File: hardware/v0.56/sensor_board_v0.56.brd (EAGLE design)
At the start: 50.8 x 50.8 mm, 69 parts, among them J3 USB-MICROB, U1 NEOPIXEL_NANO_2427, U10 TSL2591, U11 915MHz, U12 MH-Z19, U13 CCS811-I2C, U14 IAQ-CORE-C, U15 VLP-450-F, U16 VLP-450-F, U2 FT231XQ-R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

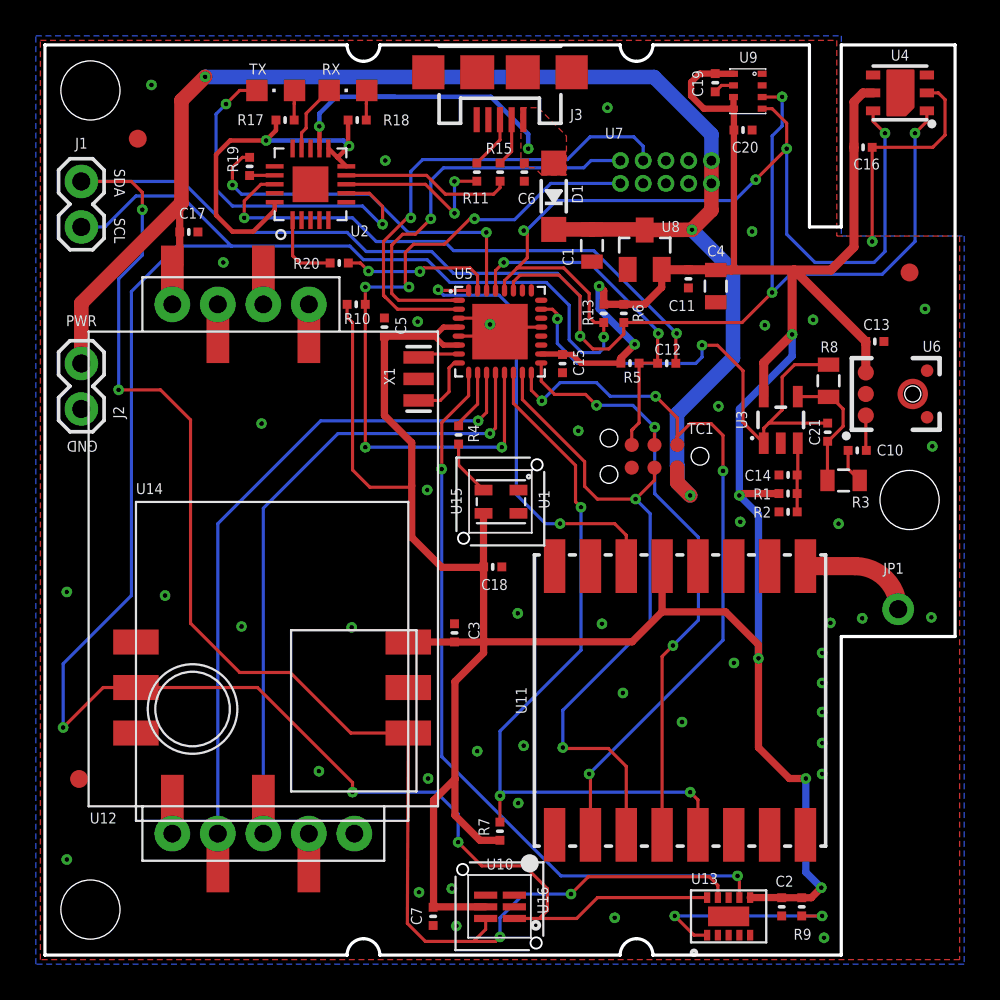
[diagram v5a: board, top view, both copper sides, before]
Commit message: v0.56b - minor update
silkscreen update and a couple of traces
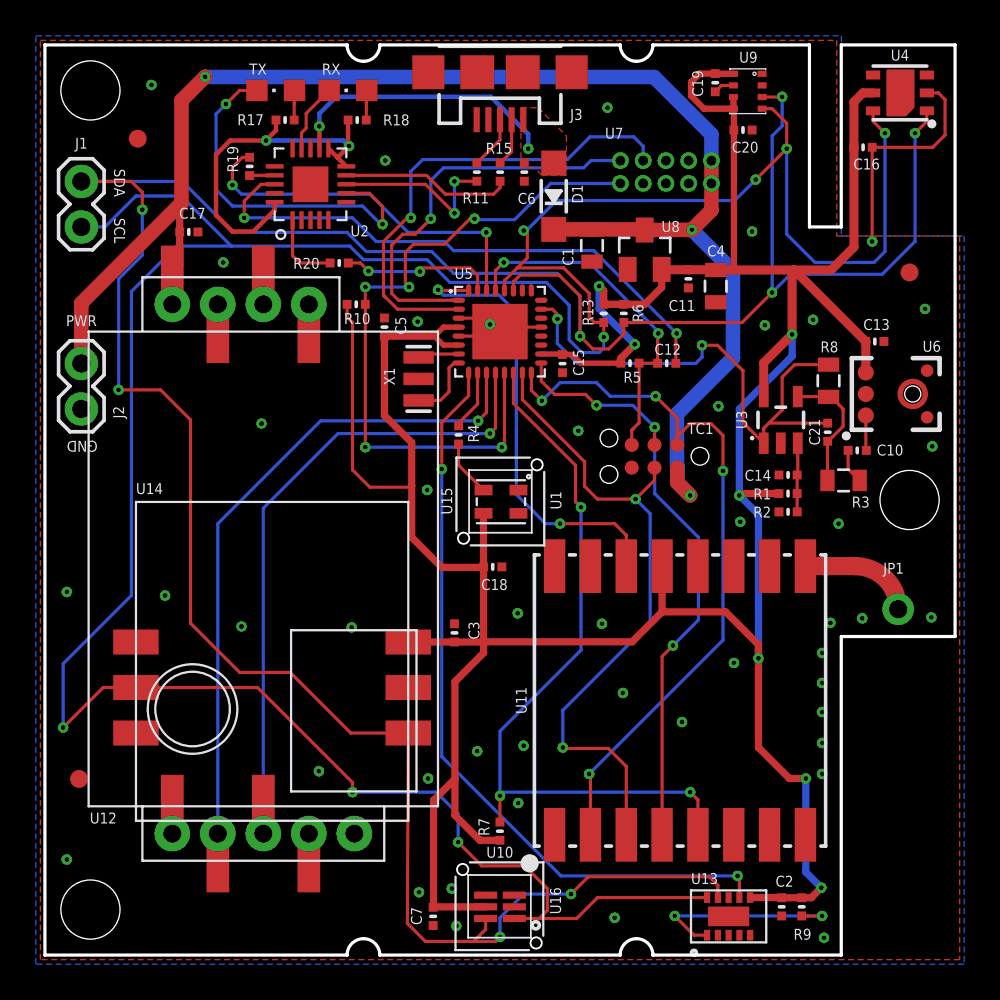
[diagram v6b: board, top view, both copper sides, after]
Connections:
- removed net N$12: U$4.P$4
- removed net N$14: U$5.P$1
- removed net N$19: U$5.P$4
- removed net N$8: U$4.P$3
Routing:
- net VBUS: track 17.8 -> 15.7 mm
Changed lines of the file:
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@@
 <element name="U10" library="TSL2591" package="DFN6_TAOS" value="TSL2591" x="25.4" y="2.6924" smashed="yes" rot="R180">
 <attribute name="MPN" value="TSL25911FN " x="25.4" y="2.6924" size="1.778" layer="27" rot="R180" display="off"/>
-<attribute name="NAME" x="24.638" y="4.7736" size="0.6096" layer="121" font="vector"/>
+<attribute name="NAME" x="24.638" y="5.434" size="0.6096" layer="121" font="vector"/>
 </element>
 <element name="J1" library="SparkFun-Connectors" package="1X02" value="" x="2.032" y="40.64" smashed="yes" rot="R90">
@@
 </element>
 <element name="U1" library="NeoPixel Nano 2427" package="SK6805-2427" value="NEOPIXEL_NANO_2427" x="24.1046" y="24.1046" smashed="yes">
-<attribute name="NAME" x="28.1686" y="24.9174" size="0.6096" layer="121" font="vector" rot="R90"/>
+<attribute name="NAME" x="28.829" y="24.8666" size="0.6096" layer="121" font="vector" rot="R90"/>
 </element>
 <element name="C18" library="Adafruit Feather 32u4 Bluefruit LE" package="MICROBUILDER__0402MP" value="1uF" x="24.9936" y="21.6662" smashed="yes" rot="R180">
@@
 </element>
 <element name="U15" library="VLP-450-F" package="VLP-450-F" value="VLP-450-F" x="23.368" y="23.2664" smashed="yes">
-<attribute name="NAME" x="23.2664" y="24.5872" size="0.6096" layer="121" font="vector" rot="R90"/>
+<attribute name="NAME" x="22.733" y="24.5872" size="0.6096" layer="121" font="vector" rot="R90"/>
 </element>
 <element name="U16" library="VLP-450-F" package="VLP-450-F" value="VLP-450-F" x="23.3172" y="4.7752" smashed="yes" rot="R270">
-<attribute name="NAME" x="27.4828" y="3.81" size="0.6096" layer="121" font="vector" rot="R270"/>
+<attribute name="NAME" x="28.194" y="3.7846" size="0.6096" layer="121" font="vector" rot="R270"/>
 </element>
 <element name="C5" library="Adafruit Feather 32u4 Bluefruit LE" package="MICROBUILDER__0402MP" value="0.1uF" x="18.9484" y="35.052" smashed="yes" rot="R270">
@@
 <vertex x="26.5684" y="43.942"/>
 </polygon>
-<wire x1="17.4752" y1="47.9044" x2="24.892" y2="47.9044" width="0.254" layer="16"/>
 <wire x1="26.9748" y1="45.0088" x2="26.9748" y2="45.8216" width="0.254" layer="16"/>
 <wire x1="26.9748" y1="45.8216" x2="24.892" y2="47.9044" width="0.254" layer="16"/>
 <wire x1="15.3232" y1="45.021" x2="15.3232" y2="46.2464" width="0.254" layer="1"/>
 <wire x1="15.3232" y1="46.2464" x2="15.3162" y2="46.2534" width="0.254" layer="1"/>
-<wire x1="16.256" y1="47.9044" x2="19.5326" y2="47.9044" width="0.254" layer="16"/>
-<wire x1="15.3162" y1="46.2534" x2="15.3162" y2="46.9646" width="0.254" layer="16"/>
-<wire x1="15.3162" y1="46.9646" x2="16.256" y2="47.9044" width="0.254" layer="16"/>
-<wire x1="17.4752" y1="47.9044" x2="16.256" y2="47.9044" width="0" layer="19" extent="16-16"/>
+<wire x1="15.3162" y1="46.9646" x2="15.3162" y2="46.2534" width="0.254" layer="16"/>
+<wire x1="24.892" y1="47.9044" x2="16.256" y2="47.9044" width="0.254" layer="16"/>
+<wire x1="16.256" y1="47.9044" x2="15.3162" y2="46.9646" width="0.254" layer="16"/>
 </signal>
 <signal name="N$32">
@@
 <wire x1="45.2196" y1="21.7094" x2="47.625" y2="19.304" width="1.016" layer="1" curve="-90"/>
 </signal>
-<signal name="N$8">
-<contactref element="U$4" pad="P$3"/>
-</signal>
-<signal name="N$12">
-<contactref element="U$4" pad="P$4"/>
-</signal>
-<signal name="N$14">
-<contactref element="U$5" pad="P$1"/>
-</signal>
-<signal name="N$19">
-<contactref element="U$5" pad="P$4"/>
-</signal>
 </signals>

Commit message: Shifted radio a bit
to allow space for the light pipe to land
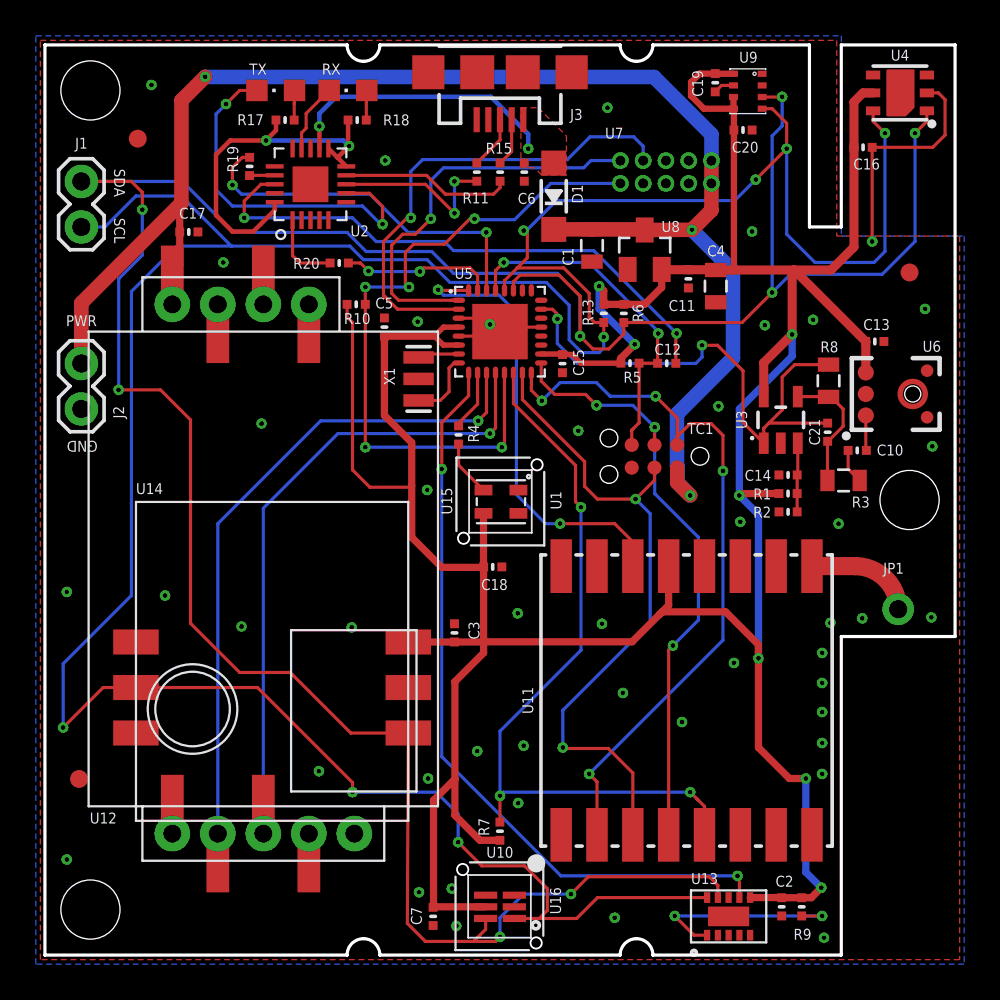
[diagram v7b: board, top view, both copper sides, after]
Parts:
- moved U11 0.37 mm to (35.8, 14.2)
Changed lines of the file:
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@@
 <attribute name="NAME" x="31.2612" y="45.5714" size="0.6096" layer="121" font="vector"/>
 </element>
-<element name="U11" library="SparkFun-RF" package="RFM69HCW-XXXS2" value="915MHz" x="35.4478" y="14.2094" smashed="yes" rot="R90">
-<attribute name="NAME" x="26.888" y="14.2094" size="0.6096" layer="121" font="vector" rot="R90" align="bottom-center"/>
-<attribute name="PROD_ID" value="IC-11997" x="35.4478" y="14.2094" size="1.778" layer="27" rot="R90" display="off"/>
+<element name="U11" library="SparkFun-RF" package="RFM69HCW-XXXS2" value="915MHz" x="35.814" y="14.2094" smashed="yes" rot="R90">
+<attribute name="NAME" x="27.2542" y="14.2094" size="0.6096" layer="121" font="vector" rot="R90" align="bottom-center"/>
+<attribute name="PROD_ID" value="IC-11997" x="35.814" y="14.2094" size="1.778" layer="27" rot="R90" display="off"/>
 </element>
 <element name="H3" library="SparkFun-Electromechanical" package="STAND-OFF" value="STAND-OFF" x="48.26" y="25.4"/>
@@
 </element>
 <element name="C5" library="Adafruit Feather 32u4 Bluefruit LE" package="MICROBUILDER__0402MP" value="0.1uF" x="18.9484" y="35.052" smashed="yes" rot="R270">
-<attribute name="NAME" x="19.5517" y="35.6362" size="0.6096" layer="121" font="vector" rot="R270"/>
+<attribute name="NAME" x="18.4404" y="36.0871" size="0.6096" layer="121" font="vector"/>
 </element>
 <element name="R10" library="Adafruit Feather 32u4 Bluefruit LE" package="MICROBUILDER__0402MP" value="10K" x="17.3736" y="36.322" smashed="yes">
@@
 <wire x1="24.4856" y1="21.6662" x2="24.4856" y2="17.485746875" width="0.4064" layer="1"/>
 <wire x1="24.4856" y1="16.8656" x2="24.4856" y2="17.485746875" width="0.4064" layer="1"/>
-<wire x1="34.4478" y1="21.7094" x2="34.4478" y2="19.157" width="0.4064" layer="1"/>
-<wire x1="32.776546875" y1="17.485746875" x2="34.4478" y2="19.157" width="0.4064" layer="1"/>
+<wire x1="34.30166875" y1="19.01086875" x2="32.776546875" y2="17.485746875" width="0.4064" layer="1"/>
+<wire x1="34.30166875" y1="19.01086875" x2="34.4478" y2="19.157" width="0.4064" layer="1"/>
 <wire x1="21.6916" y1="8.636" x2="22.8854" y2="9.8298" width="0.4064" layer="1"/>
 <wire x1="24.2776" y1="6.4056" x2="25.3956" y2="6.4056" width="0.4064" layer="1"/>
@@
 <wire x1="22.8854" y1="15.2654" x2="24.4856" y2="16.8656" width="0.4064" layer="1"/>
 <wire x1="24.4856" y1="17.485746875" x2="32.776546875" y2="17.485746875" width="0.4064" layer="1"/>
+<wire x1="34.814" y1="21.7094" x2="34.814" y2="19.5232" width="0.4064" layer="1"/>
+<wire x1="34.814" y1="19.5232" x2="34.30166875" y2="19.01086875" width="0.4064" layer="1"/>
 </signal>
 <signal name="SCL">
@@
 <via x="37.846" y="27.0256" extent="1-16" drill="0.25"/>
 <via x="30.3784" y="10.1092" extent="1-16" drill="0.25"/>
-<wire x1="30.4478" y1="6.7094" x2="30.4478" y2="10.0398" width="0.1778" layer="1"/>
-<wire x1="30.4478" y1="10.0398" x2="30.3784" y2="10.1092" width="0.1778" layer="1"/>
 <wire x1="37.846" y1="27.0256" x2="37.846" y2="29.005365625" width="0.1778" layer="1"/>
 <wire x1="37.846" y1="29.005365625" x2="37.184165625" y2="29.6672" width="0.1778" layer="1"/>
 <wire x1="37.846" y1="27.0256" x2="37.846" y2="17.5768" width="0.1778" layer="16"/>
 <wire x1="37.846" y1="17.5768" x2="30.3784" y2="10.1092" width="0.1778" layer="16"/>
+<wire x1="30.814" y1="6.7094" x2="30.814" y2="9.6736" width="0.1778" layer="1"/>
+<wire x1="30.814" y1="9.6736" x2="30.3784" y2="10.1092" width="0.1778" layer="1"/>
 </signal>
 <signal name="SCK">
@@
 <wire x1="34.0232" y1="28.4754" x2="34.0232" y2="29.4512" width="0.1778" layer="1"/>
 <wire x1="34.0232" y1="29.4512" x2="34.036" y2="29.464" width="0.1778" layer="1"/>
-<wire x1="34.4478" y1="16.6678" x2="34.4478" y2="6.7094" width="0.1778" layer="1"/>
 <via x="35.052" y="17.272" extent="1-16" drill="0.25"/>
 <wire x1="34.036" y1="25.7556" x2="36.4744" y2="23.3172" width="0.1778" layer="16"/>
 <wire x1="34.036" y1="25.7556" x2="34.036" y2="29.464" width="0.1778" layer="16"/>
-<wire x1="35.052" y1="17.272" x2="34.4478" y2="16.6678" width="0.1778" layer="1"/>
 <wire x1="36.4744" y1="23.3172" x2="36.4744" y2="18.6944" width="0.1778" layer="16"/>
 <wire x1="36.4744" y1="18.6944" x2="35.052" y2="17.272" width="0.1778" layer="16"/>
+<wire x1="34.814" y1="6.7094" x2="34.814" y2="17.034" width="0.1778" layer="1"/>
+<wire x1="34.814" y1="17.034" x2="35.052" y2="17.272" width="0.1778" layer="1"/>
 </signal>
 <signal name="RESET">
@@
 <wire x1="26.65" y1="32.498" x2="26.65" y2="31.008" width="0.1778" layer="1"/>
 <wire x1="26.65" y1="31.008" x2="30.1244" y2="27.5336" width="0.1778" layer="1"/>
-<wire x1="32.4478" y1="6.7094" x2="32.4478" y2="10.529" width="0.1778" layer="1"/>
-<wire x1="32.4478" y1="10.529" x2="31.4452" y2="11.5316" width="0.1778" layer="1"/>
 <wire x1="31.4452" y1="11.5316" x2="28.956" y2="11.5316" width="0.1778" layer="1"/>
 <wire x1="28.956" y1="11.5316" x2="28.9052" y2="11.5824" width="0.1778" layer="1"/>
@@
 <wire x1="33.782" y1="24.638" x2="32.9692" y2="25.4508" width="0.1778" layer="16"/>
 <via x="32.9692" y="25.4508" extent="1-16" drill="0.25"/>
+<wire x1="32.814" y1="6.7094" x2="32.814" y2="10.1628" width="0.1778" layer="1"/>
+<wire x1="32.814" y1="10.1628" x2="31.4452" y2="11.5316" width="0.1778" layer="1"/>
 </signal>
 <signal name="A0">
@@
 <wire x1="25.3956" y1="7.4216" x2="25.3956" y2="8.8856" width="0.1778" layer="1"/>
 <wire x1="25.3956" y1="8.8856" x2="25.4" y2="8.89" width="0.1778" layer="1"/>
-<wire x1="36.4478" y1="6.7094" x2="36.4478" y2="8.6626" width="0.1778" layer="1"/>
-<wire x1="36.4478" y1="8.6626" x2="36.0172" y2="9.0932" width="0.1778" layer="1"/>
+<wire x1="36.3806375" y1="8.7297625" x2="36.4478" y2="8.6626" width="0.1778" layer="1"/>
 <via x="36.0172" y="9.0932" extent="1-16" drill="0.25"/>
+<wire x1="36.3806375" y1="8.7297625" x2="36.0172" y2="9.0932" width="0.1778" layer="1"/>
 <wire x1="36.0172" y1="9.0932" x2="25.6032" y2="9.0932" width="0.1778" layer="16"/>
 <wire x1="25.6032" y1="9.0932" x2="25.4" y2="8.89" width="0.1778" layer="16"/>
+<wire x1="36.814" y1="6.7094" x2="36.814" y2="8.2964" width="0.1778" layer="1"/>
+<wire x1="36.814" y1="8.2964" x2="36.3806375" y2="8.7297625" width="0.1778" layer="1"/>
 </signal>
 <signal name="OUT">
@@
 <wire x1="28.7902" y1="24.0418" x2="28.7528" y2="24.0792" width="0.1778" layer="1"/>
 <wire x1="26.3144" y1="35.8648" x2="25.3492" y2="36.83" width="0.1778" layer="16"/>
-<wire x1="32.4478" y1="21.7094" x2="32.4478" y2="23.4322" width="0.1778" layer="1"/>
-<wire x1="31.8008" y1="24.0792" x2="32.4478" y2="23.4322" width="0.1778" layer="1"/>
-<wire x1="28.7528" y1="24.0792" x2="31.8008" y2="24.0792" width="0.1778" layer="1"/>
+<wire x1="31.8008" y1="24.0792" x2="28.7528" y2="24.0792" width="0.1778" layer="1"/>
 <wire x1="27.94" y1="24.0792" x2="26.3144" y2="25.7048" width="0.1778" layer="16"/>
 <wire x1="26.3144" y1="35.8648" x2="26.3144" y2="25.7048" width="0.1778" layer="16"/>
@@
 <wire x1="25.3492" y1="36.83" x2="22.2504" y2="36.83" width="0.1778" layer="16"/>
 <wire x1="22.2504" y1="36.83" x2="21.9456" y2="37.1348" width="0.1778" layer="16"/>
+<wire x1="32.814" y1="21.7094" x2="32.814" y2="23.066" width="0.1778" layer="1"/>
+<wire x1="32.814" y1="23.066" x2="31.8008" y2="24.0792" width="0.1778" layer="1"/>
 </signal>
 <signal name="D6">
@@
 <contactref element="U11" pad="9"/>
 <contactref element="JP1" pad="1"/>
-<wire x1="42.4478" y1="21.7094" x2="45.2196" y2="21.7094" width="1.016" layer="1"/>
 <wire x1="45.2196" y1="21.7094" x2="47.625" y2="19.304" width="1.016" layer="1" curve="-90"/>
+<wire x1="42.814" y1="21.7094" x2="45.2196" y2="21.7094" width="1.016" layer="1"/>
 </signal>
 </signals>
